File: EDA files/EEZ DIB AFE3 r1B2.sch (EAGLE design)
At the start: 179 parts, among them IC1 AMC3330QDWERQ1, IC10 N.C., IC11 ADS131E04IPAGR, IC12 TPS71725DCKR, IC13 TPS72325DBVR, IC2 ULN2803ADWR, IC3 AMC3301DWER, IC4 MCP6004T-I/ST, IC5 DG212BDY-T1-E3, IC6 MCP6001RT-I/OT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

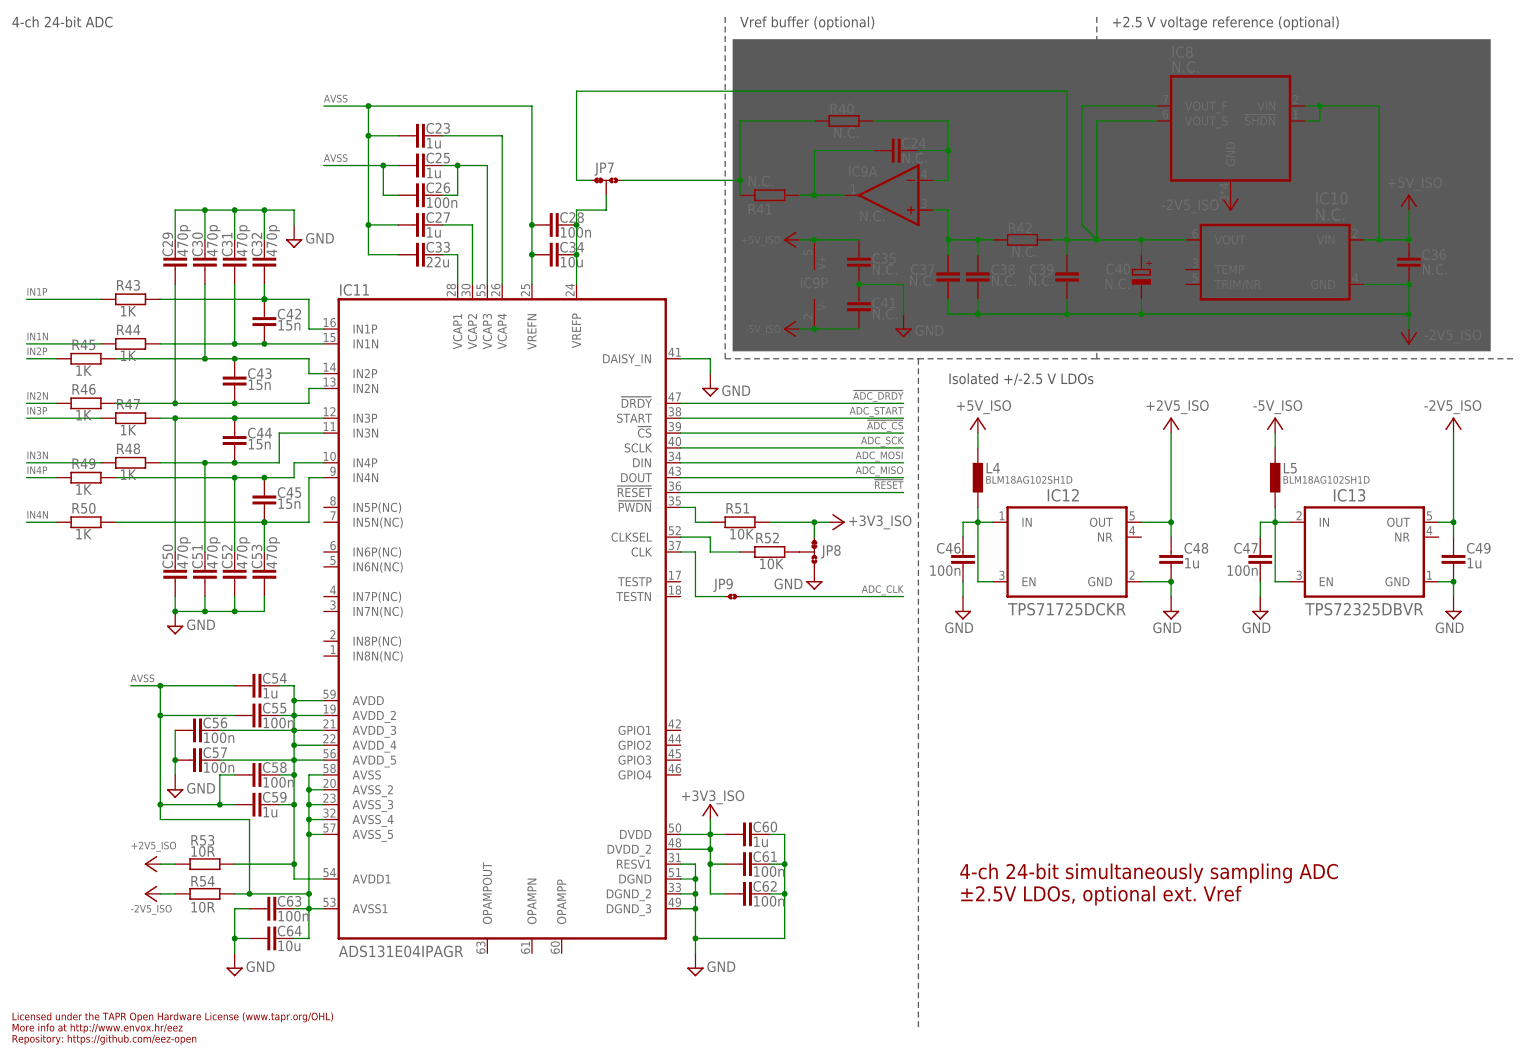
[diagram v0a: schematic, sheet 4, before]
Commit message: r1B2 (removed RC from ADC inputs)
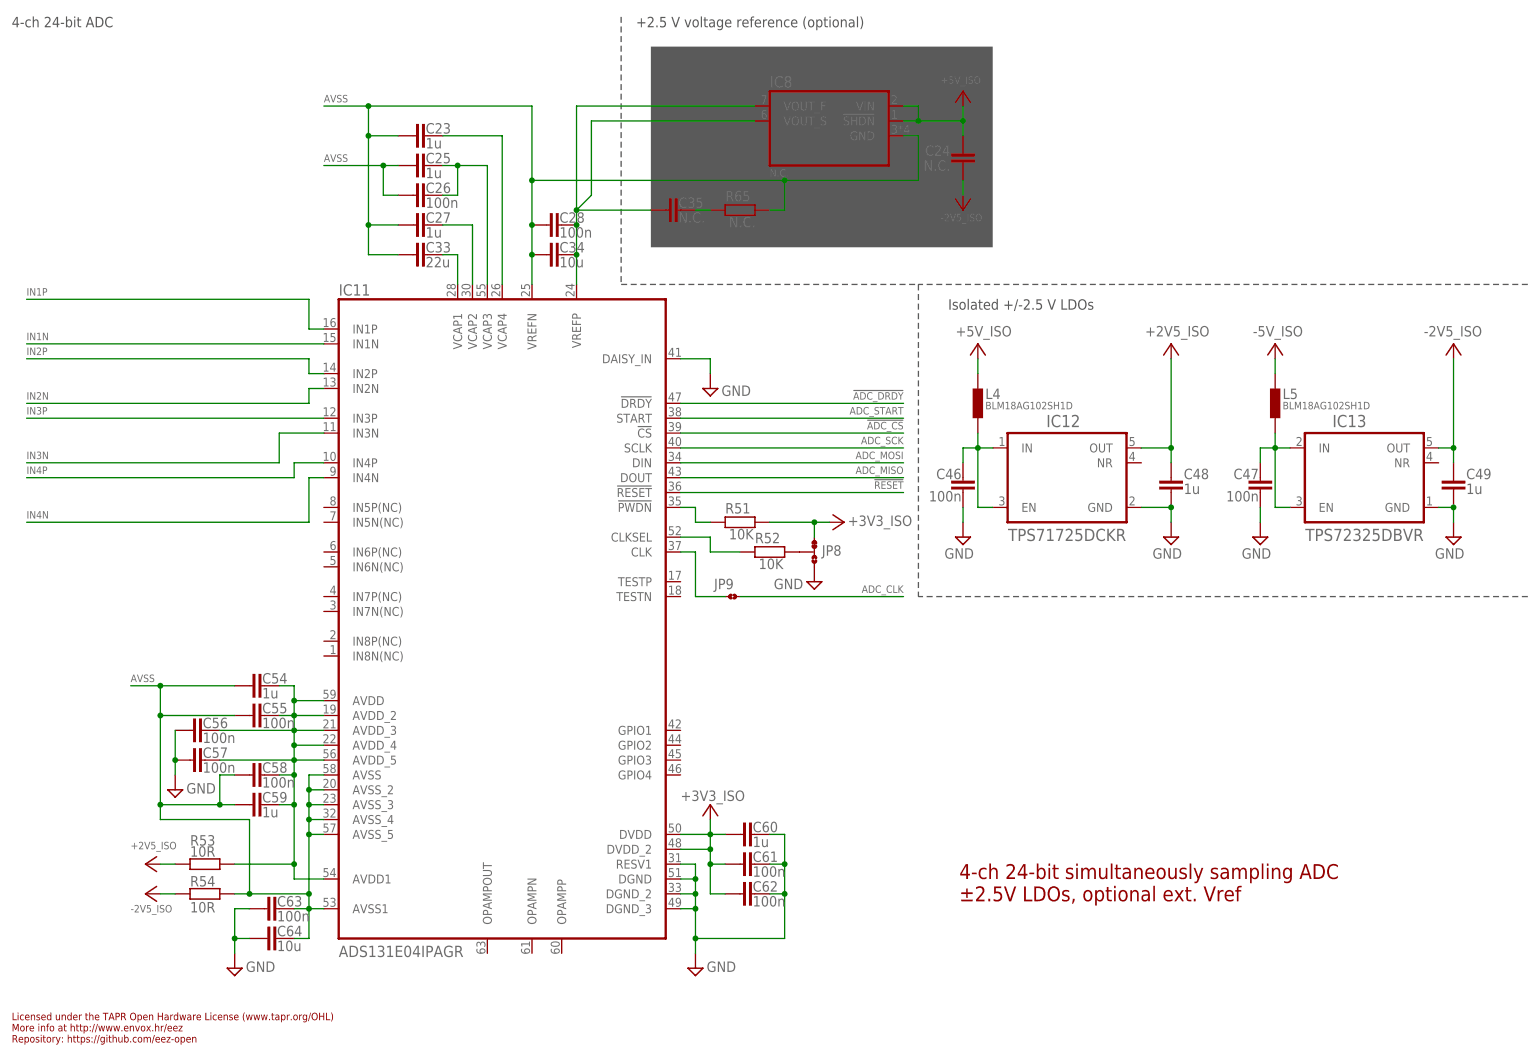
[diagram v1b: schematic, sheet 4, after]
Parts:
- removed C29, C30, C31, C32, C50, C51, C52, C53: 470p, rcl:C-EUC0603
- removed C36, C37, C38, C39: N.C., rcl:C-EUC1206
- removed C40: N.C., EEZ_Lib1:ECAP1206
- removed C41: N.C., rcl:C-EUC0603
- removed C42, C43, C44, C45: 15n, rcl:C-EUC0603
- removed IC10: N.C., EEZ_TI:REF50XX
- removed IC9: N.C., EEZ_TI:OPA376AIDBVR
- removed JP7: JP3-CUT-0805-ROTATED, EEZ_Lib1:JP3-CUT-0805-ROTATED
- removed R40, R41, R42: N.C., rcl:R-EU_R0805
- removed R43, R44, R45, R46, R47, R48, R49, R50: 1K, rcl:R-EU_R0805
- added R65: N.C., rcl:R-EU_R0805
- C24: device rcl:C-EUC0805 -> rcl:C-EUC1206
- C35: device rcl:C-EUC0603 -> rcl:C-EUC1206
- F5: value ZH32 (1A) -> ZH32 (1.25A)
- IC6: value MCP6001RT-I/OT -> MCP6001T-I/OT
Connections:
- removed net IN1+: C32.2, C42.2, IC11.IN1P, R43.2
- removed net IN1-: C31.2, C42.1, IC11.IN1N, R44.2
- removed net IN2+: C30.2, C43.2, IC11.IN2P, R45.2
- removed net IN2-: C29.2, C43.1, IC11.IN2N, R46.2
- removed net IN3+: C44.2, C50.2, IC11.IN3P, R47.2
- removed net IN3-: C44.1, C51.2, IC11.IN3N, R48.2
- removed net IN4+: C45.2, C52.2, IC11.IN4P, R49.2
- removed net IN4-: C45.1, C53.2, IC11.IN4N, R50.2
- removed net N$101: C37.1, C38.1, IC9A.+IN, R42.1
- removed net N$102: C24.2, IC9A.-IN, R40.2
- removed net N$103: C24.1, IC9A.OUT, R41.2
- removed net N$104: JP7.NO, R40.1, R41.1
- net +5V_ISO: now also C24.1; no longer C35.1, C36.1, IC10.VIN, IC9P.V+
- net -2V5_ISO: now also C24.2; no longer C36.2, C37.2, C38.2, C39.2, C40.-, IC10.GND, IC8.GND
- net -5V_ISO: no longer C41.2, IC9P.V-
- net AVSS: now also IC8.GND, R65.2
- net GND: no longer C29.1, C30.1, C31.1, C32.1, C35.2, C41.1, C50.1, C51.1, C52.1, C53.1
- net IN1N: now also IC11.IN1N; no longer R44.1
- net IN1P: now also IC11.IN1P; no longer R43.1
- net IN2N: now also IC11.IN2N; no longer R46.1
- net IN2P: now also IC11.IN2P; no longer R45.1
- net IN3N: now also IC11.IN3N; no longer R48.1
- net IN3P: now also IC11.IN3P; no longer R47.1
- net IN4N: now also IC11.IN4N; no longer R50.1
- net IN4P: now also IC11.IN4P; no longer R49.1
- net N$100: now also C35.2, R65.1; no longer C39.1, C40.+, IC10.VOUT, IC8.VOUT_F, IC8.VOUT_S, JP7.NC, R42.2
- net VREFP: now also C35.1, IC8.VOUT_F, IC8.VOUT_S; no longer JP7.COM
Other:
- note added: "Current ranges: ±1 A (gain x1), ±10 A (gain x2)"
- note added: "Fixed gain: x2"
- note added: "Fixed gain: x8.2"
- note added: "Voltage ranges: ±55 V, ±480 V"
- note removed: "Tant."
- note removed: "Vref buffer (optional)"
- moved on the sheet: C24, C35, C46, C47, C48, C49, IC12, IC13, IC8, L4, L5
